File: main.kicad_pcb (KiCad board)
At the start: 2 copper layers, 13 parts, among them J4 UART, Q1 DMG1023UV-7, Q2 DMG1024UV-7, U1 USBLC6-2SC6, U2 SPX3819M5-L-3-3, U3 74LVC2T45DC, U4 74LVC2T45DC, U5 74LVC2T45DC, U6 74LVC2T45DC, U7 STM32F103CBUx

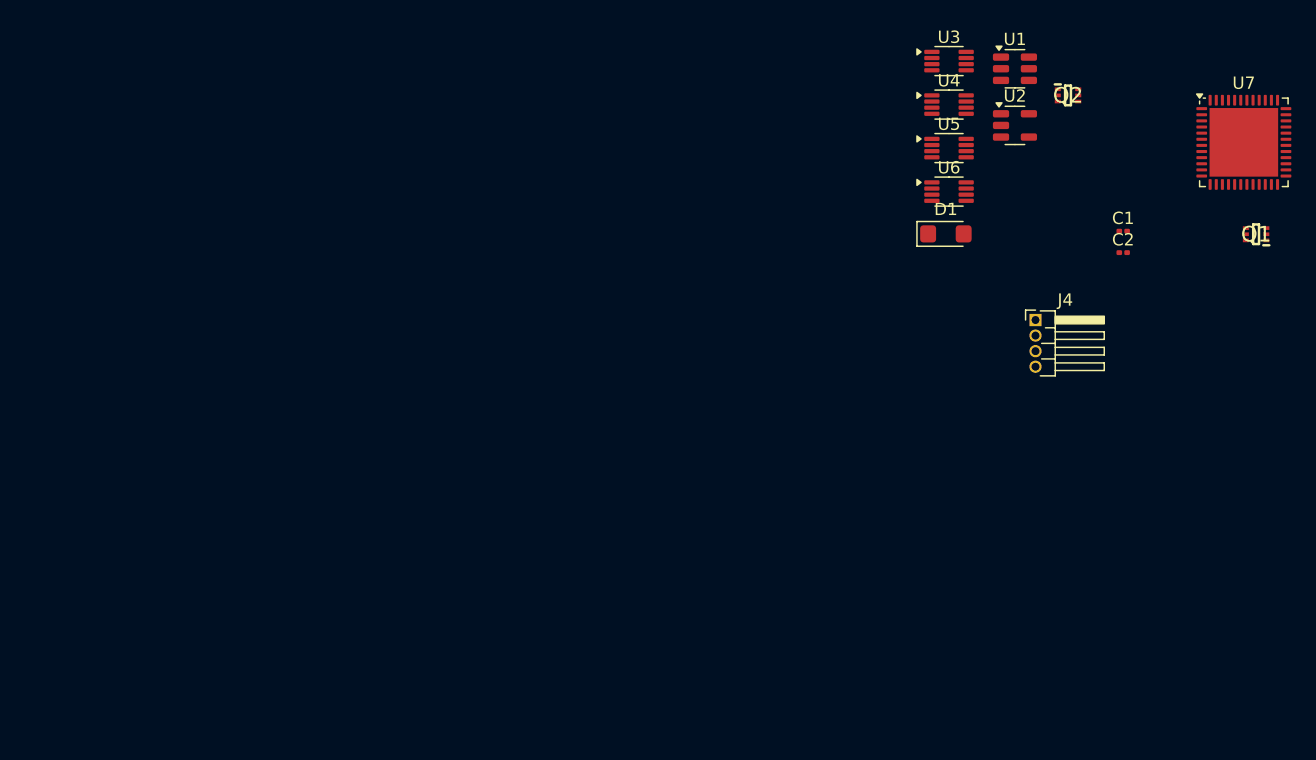
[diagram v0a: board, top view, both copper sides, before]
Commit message: layout: initial design with added LCSC part metadata
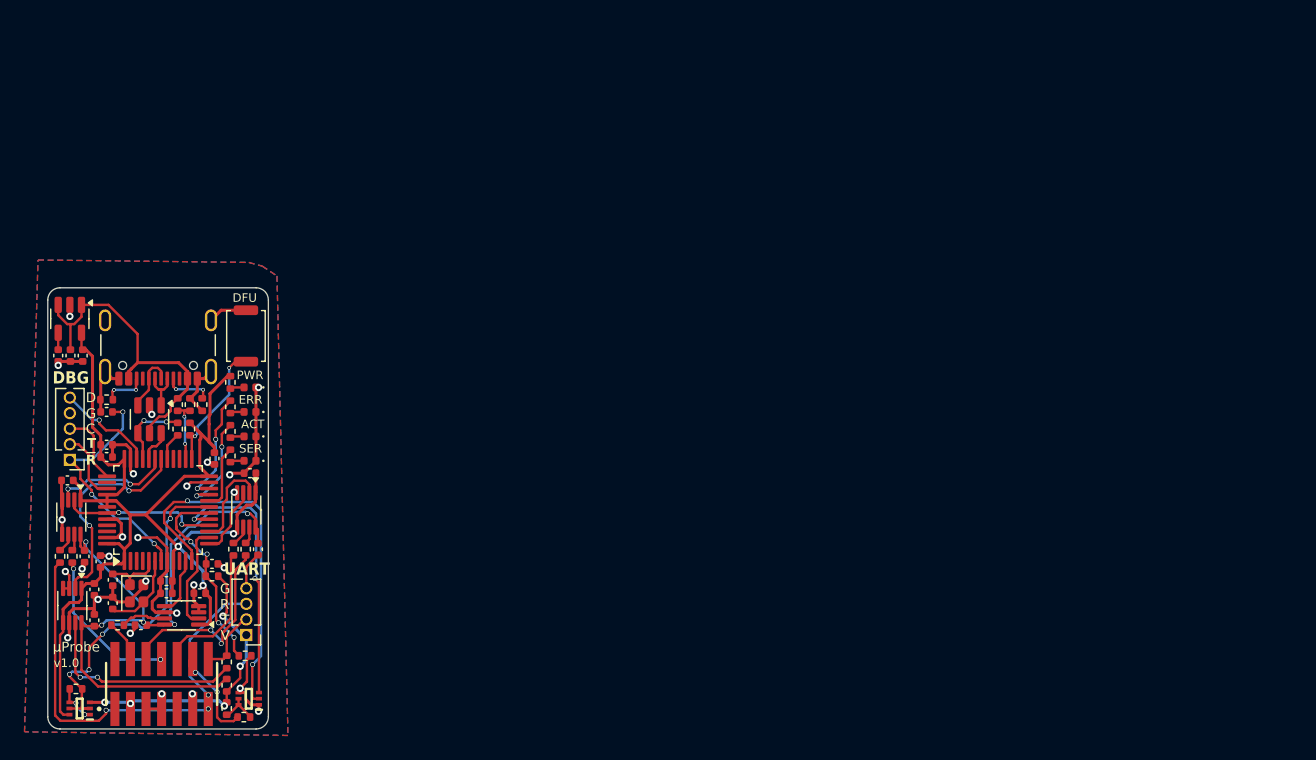
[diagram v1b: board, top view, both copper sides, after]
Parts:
- added C10: 100n, Capacitor_SMD:C_0402_1005Metric, F.Cu at (70.2, 110.5)
- added C11: 100n, Capacitor_SMD:C_0402_1005Metric, F.Cu at (70.2, 113.0)
- added C12: 100n, Capacitor_SMD:C_0402_1005Metric, F.Cu at (78.8, 110.8)
- added C13: 100n, Capacitor_SMD:C_0402_1005Metric, F.Cu at (74.0, 113.4)
- added C14: 1u, Capacitor_SMD:C_0402_1005Metric, F.Cu at (76.1, 110.8)
- added C15: 4.7u, Capacitor_SMD:C_0402_1005Metric, F.Cu at (71.2, 99.7)
- added C16: 100n, Capacitor_SMD:C_0402_1005Metric, F.Cu at (76.1, 109.8)
- added C17: 100n, Capacitor_SMD:C_0402_1005Metric, F.Cu at (80.0, 99.8)
- added C18: 100n, Capacitor_SMD:C_0402_1005Metric, F.Cu at (71.2, 98.7)
- added C19: 100n, Capacitor_SMD:C_0402_1005Metric, F.Cu at (70.7, 108.2)
- added C20: 12p, Capacitor_SMD:C_0402_1005Metric, F.Cu at (71.7, 111.6)
- added C21: 12p, Capacitor_SMD:C_0402_1005Metric, F.Cu at (71.7, 109.7)
- added C3: 4.7u, Capacitor_SMD:C_0402_1005Metric, F.Cu at (68.2, 91.4)
- added C4: 10n, Capacitor_SMD:C_0402_1005Metric, F.Cu at (67.2, 91.4)
- added C5: 4.7u, Capacitor_SMD:C_0402_1005Metric, F.Cu at (69.2, 91.4)
- added C6: 100n, Capacitor_SMD:C_0402_1005Metric, F.Cu at (68.0, 101.6)
- added C7: 100n, Capacitor_SMD:C_0402_1005Metric, F.Cu at (69.4, 107.8)
- added C8: 100n, Capacitor_SMD:C_0402_1005Metric, F.Cu at (82.9, 101.0)
- added C9: 100n, Capacitor_SMD:C_0402_1005Metric, F.Cu at (83.5, 107.2)
- added D2: ORANGE, LED_SMD:LED_0402_1005Metric, F.Cu at (82.9, 100.0)
- added D3: RED, LED_SMD:LED_0402_1005Metric, F.Cu at (82.9, 96.0)
- added D4: YELLOW, LED_SMD:LED_0402_1005Metric, F.Cu at (82.9, 98.0)
- added J1: USB_C_Receptacle_USB2.0_16P, Connector_USB:USB_C_Receptacle_GCT_USB4105-xx-A_16P_TopMnt_Horizontal, F.Cu at (75.4, 89.6)
- added J2: Conn_ST_STDC14, footprints:SAMTEC_FTSH-107-01-L-DV-K, F.Cu at (75.7, 118.2)
- added J3: DEBUG, Connector_PinHeader_1.27mm:PinHeader_1x05_P1.27mm_Vertical, F.Cu at (68.2, 99.9)
- added R1: 4.7k, Resistor_SMD:R_0402_1005Metric, F.Cu at (79.8, 109.4)
- added R10: 330, Resistor_SMD:R_0402_1005Metric, F.Cu at (81.3, 95.6)
- added R11: 330, Resistor_SMD:R_0402_1005Metric, F.Cu at (81.3, 97.6)
- added R12: 100, Resistor_SMD:R_0402_1005Metric, F.Cu at (81.0, 118.3)
- added R13: 100, Resistor_SMD:R_0402_1005Metric, F.Cu at (82.4, 120.9)
- added R14: 100, Resistor_SMD:R_0402_1005Metric, F.Cu at (82.5, 107.2)
- added R15: 100, Resistor_SMD:R_0402_1005Metric, F.Cu at (72.1, 113.4)
- added R16: 100, Resistor_SMD:R_0402_1005Metric, F.Cu at (68.4, 107.8)
- added R17: 100, Resistor_SMD:R_0402_1005Metric, F.Cu at (81.5, 107.2)
- added R18: 100, Resistor_SMD:R_0402_1005Metric, F.Cu at (67.4, 107.8)
- added R19: 100, Resistor_SMD:R_0402_1005Metric, F.Cu at (81.0, 116.4)
- added R2: 10k, Resistor_SMD:R_0402_1005Metric, F.Cu at (82.5, 115.9)
- added R20: 4.7k, Resistor_SMD:R_0402_1005Metric, F.Cu at (77.0, 95.4)
- added R21: 10k, Resistor_SMD:R_0402_1005Metric, F.Cu at (78.0, 95.4)
- added R22: 1.5k, Resistor_SMD:R_0402_1005Metric, F.Cu at (77.0, 97.4)
- added R3: 10k, Resistor_SMD:R_0402_1005Metric, F.Cu at (78.0, 97.4)
- added R4: 5.1k, Resistor_SMD:R_0402_1005Metric, F.Cu at (79.0, 95.4)
- added R5: 5.1k, Resistor_SMD:R_0402_1005Metric, F.Cu at (71.2, 95.0)
- added R6: 10k, Resistor_SMD:R_0402_1005Metric, F.Cu at (68.7, 118.6)
- added R7: 10k, Resistor_SMD:R_0402_1005Metric, F.Cu at (81.0, 120.2)
- added R8: 330, Resistor_SMD:R_0402_1005Metric, F.Cu at (81.3, 93.6)
- added R9: 330, Resistor_SMD:R_0402_1005Metric, F.Cu at (81.3, 99.6)
- added SW1: DFU, Button_Switch_SMD:SW_Push_SPST_NO_Alps_SKRK, F.Cu at (82.6, 89.8)
- added Y1: 8 MHz, footprints:Crystal_4P_GND24, F.Cu at (73.7, 110.8)
- C1, C2: footprint Capacitor_SMD:C_0201_0603Metric -> Capacitor_SMD:C_0402_1005Metric
- D1: value SMF5V0A -> GREEN; footprint Diode_SMD:D_SMF -> LED_SMD:LED_0402_1005Metric
- J4: footprint Connector_PinHeader_1.27mm:PinHeader_1x04_P1.27mm_Horizontal -> Connector_PinHeader_1.27mm:PinHeader_1x04_P1.27mm_Vertical
- U7: value STM32F103CBUx -> STM32F103C8Tx; footprint Package_DFN_QFN:QFN-48-1EP_7x7mm_P0.5mm_EP5.6x5.6mm -> Package_QFP:LQFP-48_7x7mm_P0.5mm
- moved Q1 103.5 mm to (69.0, 120.2)
- moved U7 93.5 mm to (75.4, 104.0), turned to 90 degrees
- moved C2 84.0 mm to (71.2, 96.0)
- moved Q2 83.0 mm to (82.8, 119.4), turned to 180 degrees
- moved U3 80.7 mm to (68.3, 104.6), turned to -90 degrees
- moved U5 80.7 mm to (68.4, 111.8), turned to -90 degrees
- moved C1 79.2 mm to (79.8, 108.4)
- moved U2 78.7 mm to (68.2, 88.4), turned to -90 degrees
- moved U1 76.2 mm to (74.7, 96.6), turned to -90 degrees
- moved U6 71.5 mm to (77.3, 112.6), turned to 180 degrees
- moved J4 69.3 mm to (82.6, 114.2), turned to 180 degrees
- moved U4 66.2 mm to (82.6, 104.0), turned to -90 degrees
- moved D1 58.2 mm to (82.9, 94.0), turned to 180 degrees
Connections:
- net /~{SUPPLY_POWER} renamed /~{ASSERT_TVREF}
- C1 pad 1: /TVREF -> /STM32F103 MCU/TVREF
- D1 pad 1: +5V -> GND
- D1 pad 2: GND -> Net-(D1-A)
- J4 pad 2: /TX -> /cTX
- J4 pad 3: /RX -> /cRX
- Q1 pad 3: +3.3V -> /TVREF
- Q1 pad 6: /TVREF -> +3.3V
- U1 pad 1: Net-(J1-D--PadA7) -> /D-
- U1 pad 3: Net-(J1-D+-PadA6) -> /D+
- U4 pad 5: 3.3V -> +3.3V
- U5 pad 5: 3.3V -> +3.3V
- U7 pad 18: /TVREF -> /STM32F103 MCU/TVREF
- U7 pad 26: unconnected-(U7-PB13-Pad26) -> Net-(U7-PB13)
- U7 pad 29: unconnected-(U7-PA8-Pad29) -> Net-(U7-PA8)
- U7 pad 43: /STM32F103 MCU/SWO_UART_RX -> /TDO
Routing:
- net +3.3V: track 0.00 -> 97.1 mm, vias 0 -> 3
- net GND: track 0.00 -> 87.1 mm, vias 0 -> 26
- net /xVREF: track 0.00 -> 52.4 mm, vias 0 -> 5
- net /cRX: track 0.00 -> 38.0 mm, vias 0 -> 3
- net /STM32F103 MCU/TRST: track 0.00 -> 29.8 mm, vias 0 -> 2
- net /~{ASSERT_TVREF}: track 0.00 -> 28.1 mm, vias 0 -> 4
- net +5V: track 0.00 -> 26.9 mm
- net /TVREF: track 0.00 -> 24.0 mm, vias 0 -> 5
- net /TRST_SENSE: track 0.00 -> 21.7 mm, vias 0 -> 2
- net /~{RESET}: track 0.00 -> 19.7 mm, vias 0 -> 3
- net /TX: track 0.00 -> 17.7 mm, vias 0 -> 2
- net /xTX: track 0.00 -> 17.2 mm, vias 0 -> 2
- net /STM32F103 MCU/TVREF: track 0.00 -> 16.7 mm, vias 0 -> 4
- net Net-(J2-JCLK/SWCLK): track 0.00 -> 16.3 mm, vias 0 -> 2
- net Net-(J2-JTDO/SWO): track 0.00 -> 13.0 mm, vias 0 -> 2
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- added copper zone on B.Cu, net GND
- added copper zone on F.Cu, net GND
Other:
- board outline added: 18 x 36 mm
- board text added: "ACT"
- board text added: "C"
- board text added: "D"
- board text added: "DBG"
- board text added: "DEBUG"
- board text added: "DFU"
- board text added: "ERR"
- board text added: "G"
- board text added: "GND"
- board text added: "PWR"
- board text added: "R"
- board text added: "RX"
- board text added: "SER"
- board text added: "SWCLK"
- board text added: "SWDIO"
- board text added: "SWO"
- board text added: "T"
- board text added: "TX"
- board text added: "UART"
- board text added: "V"
- board text added: "VCC"
- board text added: "by Utkarsh Verma"
- board text added: "v1.0"
- board text added: "~{RESET}"
- board text added: "~{R}"
- board text added: "μProbe"

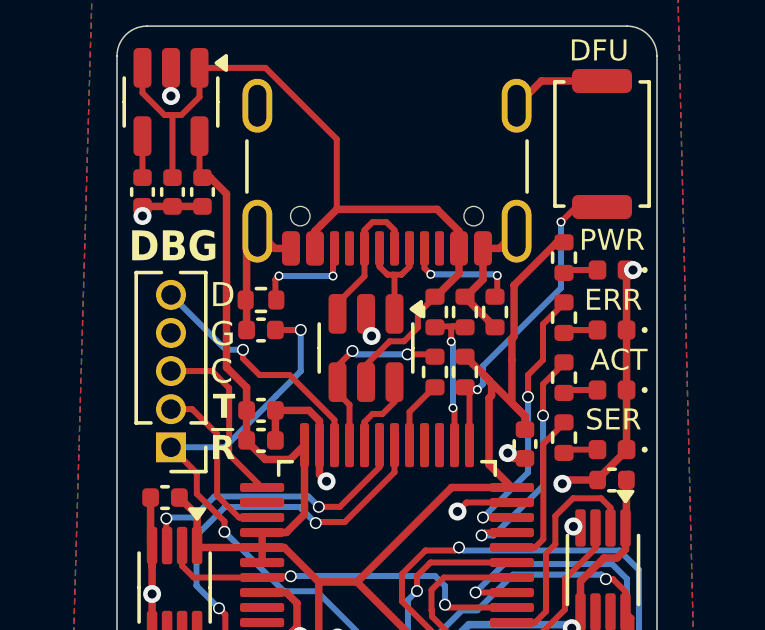
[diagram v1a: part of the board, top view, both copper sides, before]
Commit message: layout: update from schematic and add license
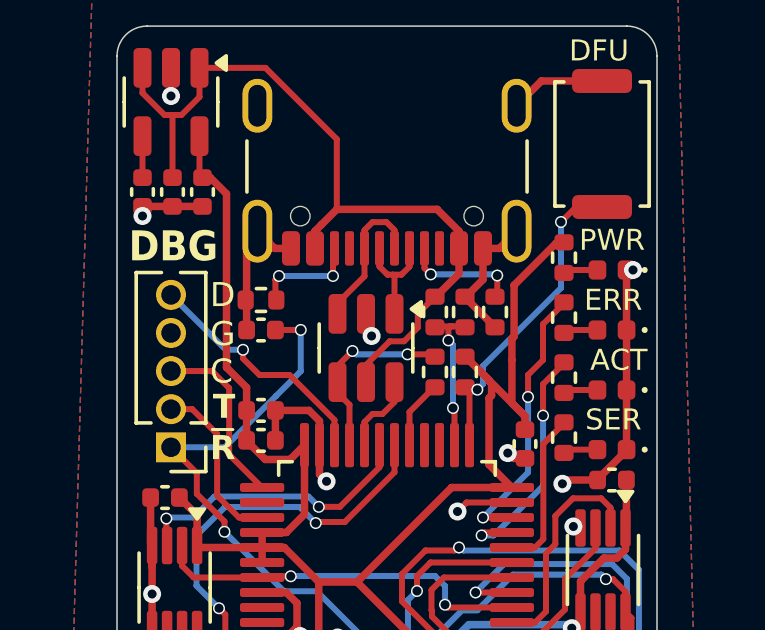
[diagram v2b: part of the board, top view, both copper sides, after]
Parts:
- U7: value STM32F103C8Tx -> STM32F103CBUx
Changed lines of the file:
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@@
 	(paper "A5" portrait)
 	(title_block
-		(title "Black Magic Probe")
+		(title "μProbe")
 		(date "2025-07-31")
-		(rev "v.10")
+		(rev "v1.0")
 		(company "Utkarsh Verma")
 		(comment 2 "(C) 2025 Utkarsh Verma")
-		(comment 3 "License: TODO")
+		(comment 3 "License: CC-BY-SA 4.0")
 	)
 	(layers
@@
 		(sheetname "/")
 		(sheetfile "main.kicad_sch")
-		(attr through_hole dnp)
+		(attr through_hole exclude_from_bom dnp)
 		(fp_line
 			(start 1.16 0.81)
@@
 			)
 		)
-		(property "Value" "STM32F103C8Tx"
+		(property "Value" "STM32F103CBUx"
 			(at 0 5.85 90)
 			(layer "F.Fab")
@@
 			)
 		)
-		(property "LCSC Part" "C14663"
+		(property "LCSC Part" "C15195"
 			(at 0 0 270)
 			(unlocked yes)
@@
 		(sheetname "/")
 		(sheetfile "main.kicad_sch")
-		(attr through_hole dnp)
+		(attr through_hole exclude_from_bom dnp)
 		(fp_line
 			(start 1.16 0.81)
@@
 	(via
 		(at 81.2 92.4)
-		(size 0.3)
-		(drill 0.2)
+		(size 0.4)
+		(drill 0.3)
 		(layers "F.Cu" "B.Cu")
 		(net 33)
@@
 	(via
 		(at 78.410576 97.989424)
-		(size 0.3)
-		(drill 0.2)
+		(size 0.4)
+		(drill 0.3)
 		(layers "F.Cu" "B.Cu")
 		(net 33)
@@
 	(via
 		(at 71.8 94.2)
-		(size 0.3)
-		(drill 0.2)
+		(size 0.4)
+		(drill 0.3)
 		(layers "F.Cu" "B.Cu")
 		(net 54)
@@
 	(via
 		(at 73.6 94.2)
-		(size 0.3)
-		(drill 0.2)
+		(size 0.4)
+		(drill 0.3)
 		(layers "F.Cu" "B.Cu")
 		(net 54)
@@
 	(via
 		(at 79.075 94.18351)
-		(size 0.3)
-		(drill 0.2)
+		(size 0.4)
+		(drill 0.3)
 		(layers "F.Cu" "B.Cu")
 		(net 55)
@@
 	(via
 		(at 76.858075 94.146085)
-		(size 0.3)
-		(drill 0.2)
+		(size 0.4)
+		(drill 0.3)
 		(layers "F.Cu" "B.Cu")
 		(net 55)
@@
 	)
 	(segment
-		(start 77.540026 96.384434)
-		(end 77.540026 95.939974)
+		(start 77.446409 96.346362)
+		(end 77.446409 95.933591)
 		(width 0.2)
 		(layer "F.Cu")
@@
 	)
 	(segment
-		(start 77.540026 95.939974)
-		(end 77.6 95.88)
+		(start 77.446409 95.933591)
+		(end 77.5 95.88)
+		(width 0.2)
+		(layer "F.Cu")
+		(net 65)
+	)
+	(segment
+		(start 77 95.88)
+		(end 77.5 95.88)
 		(width 0.2)
 		(layer "F.Cu")
@@
 	)
 	(segment
-		(start 77 95.88)
+		(start 77.5 95.88)
 		(end 77.6 95.88)
 		(width 0.2)
@@
 	)
 	(via
-		(at 77.540026 96.384434)
-		(size 0.3)
-		(drill 0.2)
+		(at 77.6 98.6)
+		(size 0.4)
+		(drill 0.3)
 		(layers "F.Cu" "B.Cu")
 		(net 65)
 	)
 	(via
-		(at 77.6 98.6)
-		(size 0.3)
-		(drill 0.2)
+		(at 77.446409 96.346362)
+		(size 0.4)
+		(drill 0.3)
 		(layers "F.Cu" "B.Cu")
 		(net 65)
 	)
 	(segment
-		(start 77.6 96.444408)
-		(end 77.540026 96.384434)
+		(start 77.6 98.6)
+		(end 77.6 96.499953)
 		(width 0.2)
 		(layer "B.Cu")
@@
 	)
 	(segment
-		(start 77.6 98.6)
-		(end 77.6 96.444408)
+		(start 77.6 96.499953)
+		(end 77.446409 96.346362)
 		(width 0.2)
 		(layer "B.Cu")
